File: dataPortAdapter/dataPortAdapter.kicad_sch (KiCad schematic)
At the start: 3 parts, among them J1 Conn_02x05_Odd_Even, J2 Conn_02x07_Odd_Even, J3 Conn_01x07

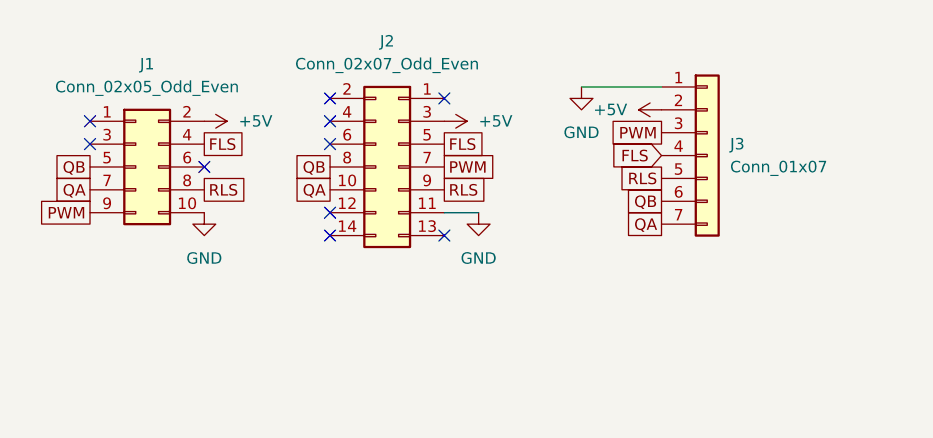
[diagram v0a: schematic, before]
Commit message: Add solder jumpers to switch between modes
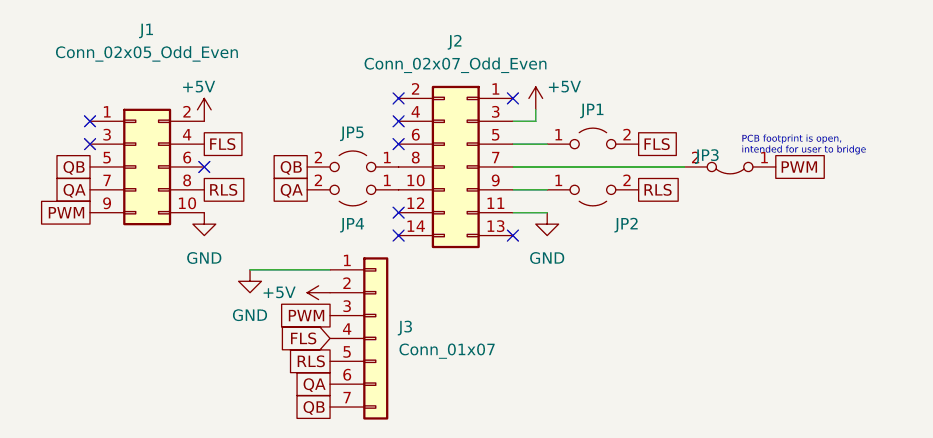
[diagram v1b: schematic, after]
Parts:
- added JP1, JP2, JP4, JP5: Jumper_2_Open, Jumper:SolderJumper-2_P1.3mm_Open_TrianglePad1.0x1.5mm, symbol Jumper:Jumper_2_Open
- added JP3: Jumper_2_Bridged, Jumper:SolderJumper-2_P1.3mm_Open_TrianglePad1.0x1.5mm, symbol Jumper:Jumper_2_Bridged
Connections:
- net FLS: now also JP1.2 (B); no longer J2.5 (Pin_5)
- net PWM: now also JP3.1 (A); no longer J2.7 (Pin_7)
- net QA: now also J3.6 (Pin_6), JP4.2 (B); no longer J2.10 (Pin_10), J3.7 (Pin_7)
- net QB: now also J3.7 (Pin_7), JP5.2 (B); no longer J2.8 (Pin_8), J3.6 (Pin_6)
- net RLS: now also JP2.2 (B); no longer J2.9 (Pin_9)
- new net: J2.5 (Pin_5), JP1.1 (A)
- new net: J2.9 (Pin_9), JP2.1 (A)
- new net: J2.10 (Pin_10), JP4.1 (A)
- new net: J2.7 (Pin_7), JP3.2 (B)
- new net: J2.8 (Pin_8), JP5.1 (A)
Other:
- note added: "PCB footprint is open, intended for user to bridge"
- moved on the sheet: J2, J3
